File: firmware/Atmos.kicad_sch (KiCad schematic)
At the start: 55 parts, among them J1 AS3935 breakout, J2 BME280 breakout, J3 USB_C_Receptacle_USB2.0_16P, J4 Micro_SD_Card, J5 Solar power input, J6 Conn_Coaxial, Q1 PMOS_Substrate, Q2 PMOS_Substrate, Q3 PMOS_Substrate, SW2 SW_Push, U1 ESP32-S3-WROOM-1, U10 TPS22918DBVR, U11 MAX17048G_T10, U12 CN3791, U13 SGP40-D-R4, U2 AP2112K-3.3, U3 DS3231M, U4 PMS5003, U5 LTC4412xS6, U7 RFM95W-915S2, U8 USBLC6-2SC6, U9 TPS61023DRLR

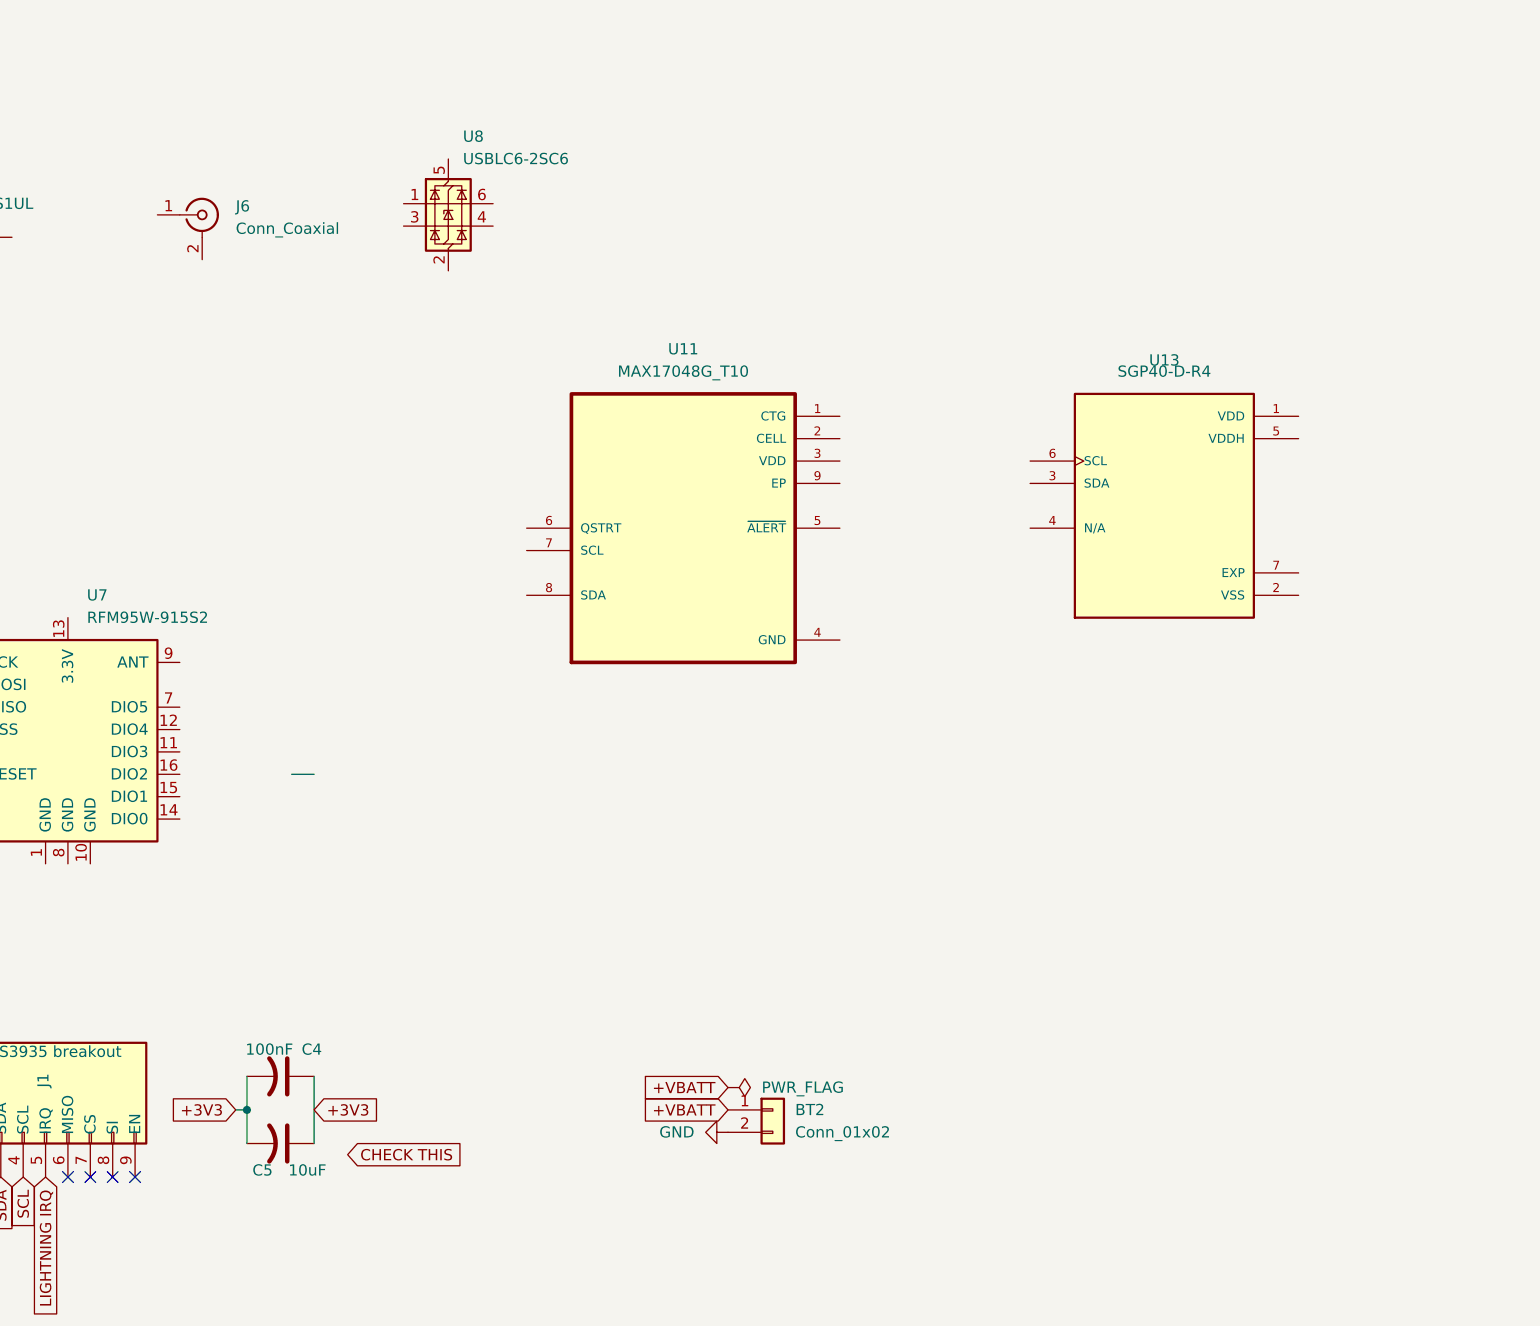
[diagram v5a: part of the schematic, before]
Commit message: U11 wired
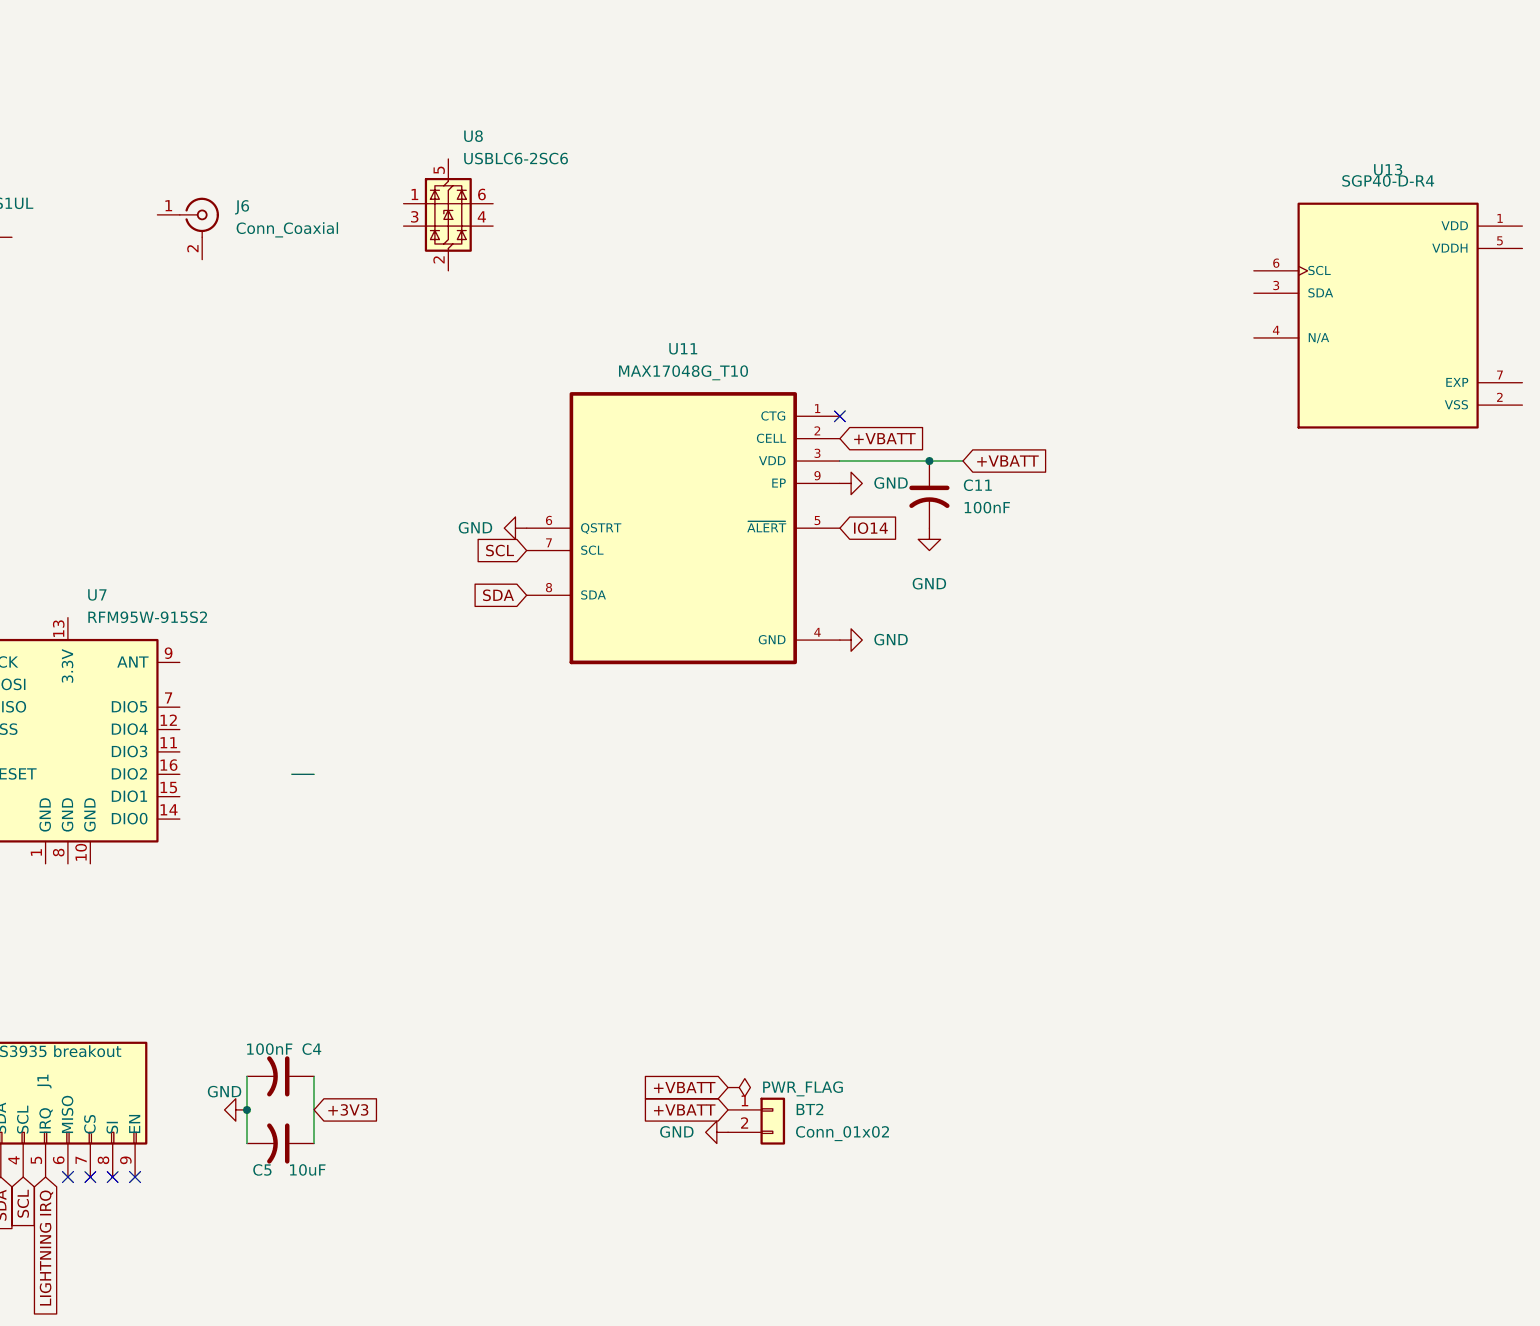
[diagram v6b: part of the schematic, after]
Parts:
- added C11: 100nF, symbol Device:C_US
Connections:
- net +3V3: no longer C4.2, C5.2
- net +VBATT: now also U11.2 (CELL), U11.3 (VDD), C11.1
- net GND: now also C4.2, C5.2, U11.4 (GND), U11.6 (QSTRT), U11.9 (EP), C11.2
- net SCL: now also U11.7 (SCL)
- net SDA: now also U11.8 (SDA)
- net IO14: now reaches U11.5 (~{ALERT})
- no-connect marks 41 -> 42
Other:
- moved on the sheet: U13

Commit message: U11 touchup
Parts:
- added C13: 1pF, symbol Device:C_US
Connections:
- net GND: now also C13.2; no longer C11.2
- new net: C11.2, C13.1
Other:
- moved on the sheet: C11, U11

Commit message: TPS init
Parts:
- added C14: 4.7uF, symbol Device:C_US
- added C15: 22uF, symbol Device:C_US
- added L2: 1uH, symbol Device:L
- added R13: 100k, symbol Device:R_US
- C13: value 1pF -> 1uF
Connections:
- net +VBATT: now also C13.1, U9.3 (VIN), C14.2
- net GND: now also C11.2, U9.4 (GND), C14.1, C15.1, R13.1
- net FB_BOOST: now reaches U9.1 (FB)
- net IO16: now reaches U9.2 (EN)
- net IO16: now also R13.2
- net at U9.5 (SW): now also L2.1
- net +5V: now reaches U9.6 (VOUT)
- net +5V: now also C15.2
- new net SW_BOOST: L2.2
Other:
- moved on the sheet: C11, C13, U11, U9
